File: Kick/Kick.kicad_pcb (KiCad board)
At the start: 4 copper layers, 127.8 x 66 mm, 11 parts, among them J1 CN1 / J11, J2 CN2 / J12, U0 NOIP1SN1300A-QTI, U1 NOIP1SN1300A-QTI, U2 NX3L4053, U3 NX3L4053, U4 MIC5504-1.8YM5

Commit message: added mounting holes for lens holder and rerouted long bottom traces from J11
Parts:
- added REF**: MountingHole_2.2mm_M2, MountingHole:MountingHole_2.2mm_M2, F.Cu at (130.9, 83.4)
- added REF**: MountingHole_2.2mm_M2, MountingHole:MountingHole_2.2mm_M2, F.Cu at (30.9, 63.4)
- added REF**: MountingHole_2.2mm_M2, MountingHole:MountingHole_2.2mm_M2, F.Cu at (50.9, 83.3)
- added REF**: MountingHole_2.2mm_M2, MountingHole:MountingHole_2.2mm_M2, F.Cu at (150.9, 63.4)
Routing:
- net /vddpix_0: track 57.8 -> 59.2 mm

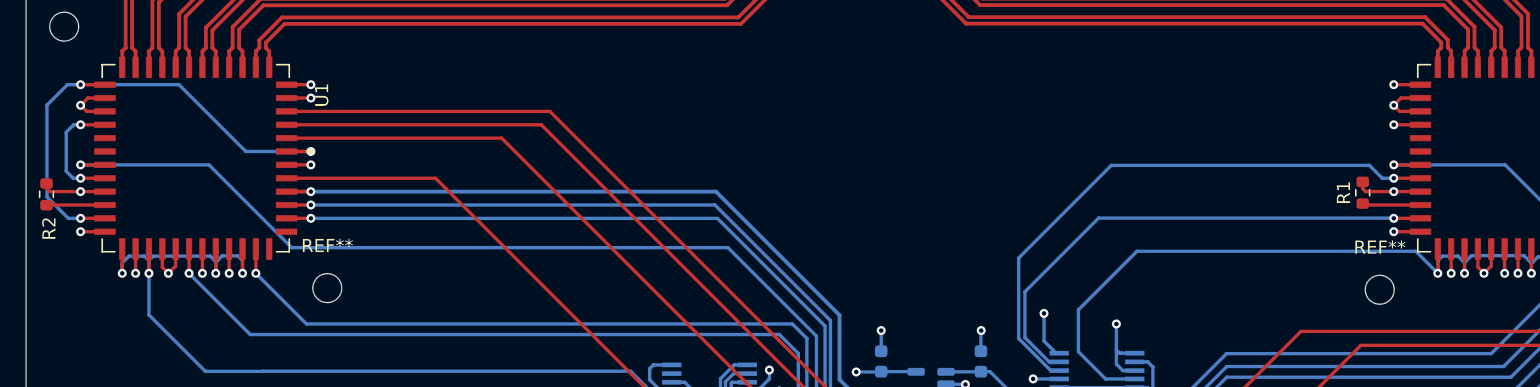
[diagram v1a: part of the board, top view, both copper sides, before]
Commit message: validated skew of single-ended signals with new clock delays
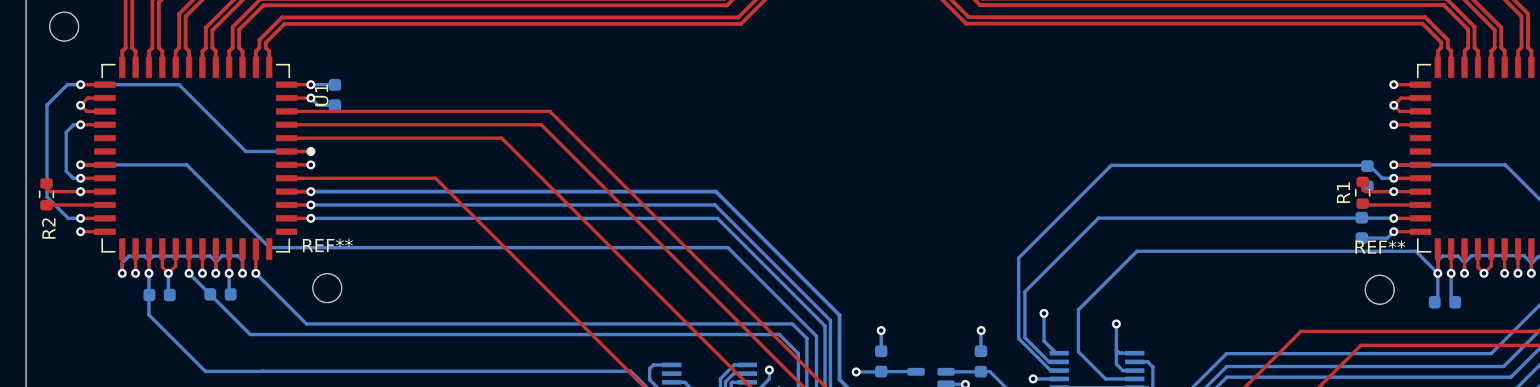
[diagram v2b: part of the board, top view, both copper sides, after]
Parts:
- added C3: C, Capacitor_SMD:C_0603_1608Metric, B.Cu at (129.5, 78.7)
- added C4: C, Capacitor_SMD:C_0603_1608Metric, B.Cu at (129.9, 74.8)
- added C5: C, Capacitor_SMD:C_0603_1608Metric, B.Cu at (135.8, 84.3)
- added C6: C, Capacitor_SMD:C_0603_1608Metric, B.Cu at (42.8, 83.8)
- added C7: C, Capacitor_SMD:C_0603_1608Metric, B.Cu at (51.5, 68.6)
- added C8: C, Capacitor_SMD:C_0603_1608Metric, B.Cu at (38.1, 83.8)
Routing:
- net GND: track 160.4 -> 173.0 mm
- net /vddpix_0: track 59.2 -> 61.5 mm
- net /vdd18_1: track 78.6 -> 80.5 mm

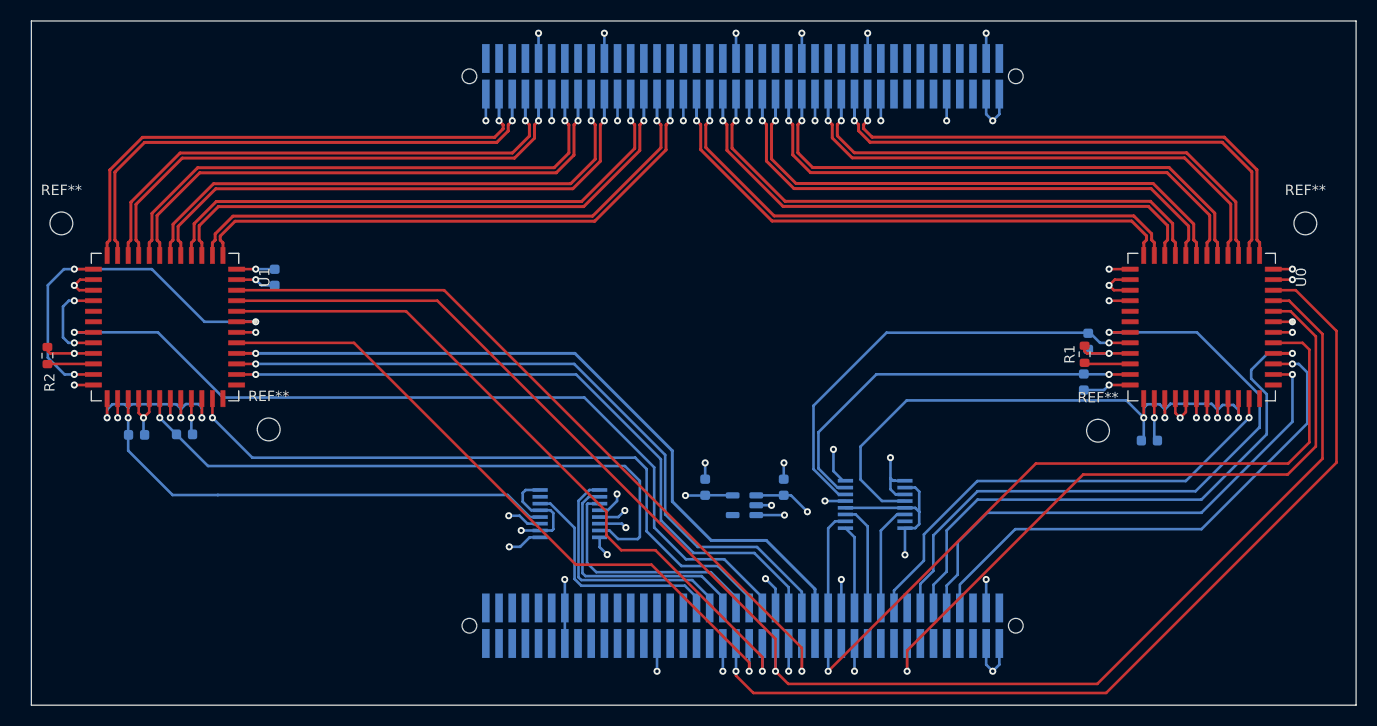
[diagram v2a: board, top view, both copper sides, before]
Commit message: length-matched spi signals
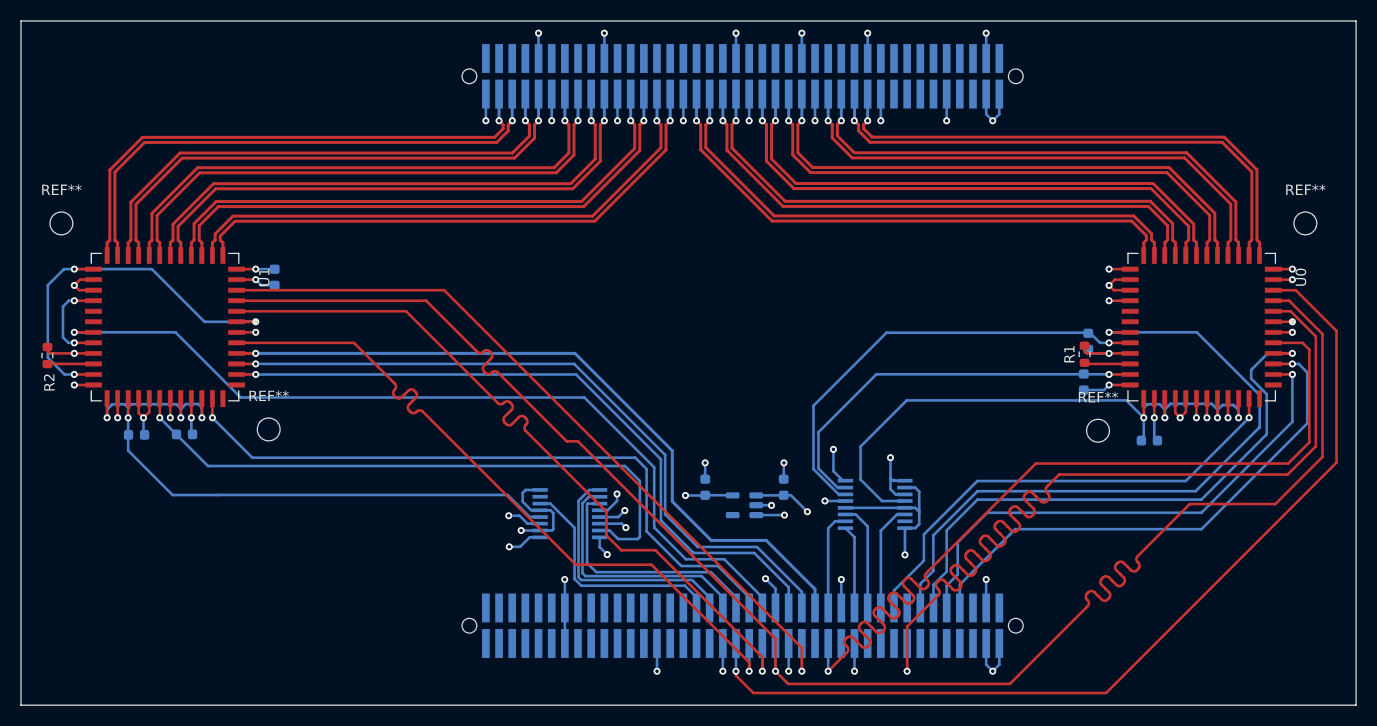
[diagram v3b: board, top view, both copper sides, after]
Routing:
- net /mosi: track 153.0 -> 179.6 mm
- net /ss_0: track 70.9 -> 86.8 mm
- net /miso: track 151.7 -> 162.1 mm
- net /ss_1: track 65.7 -> 69.4 mm
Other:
- board size 127.8 x 66 mm -> 128.8 x 66 mm

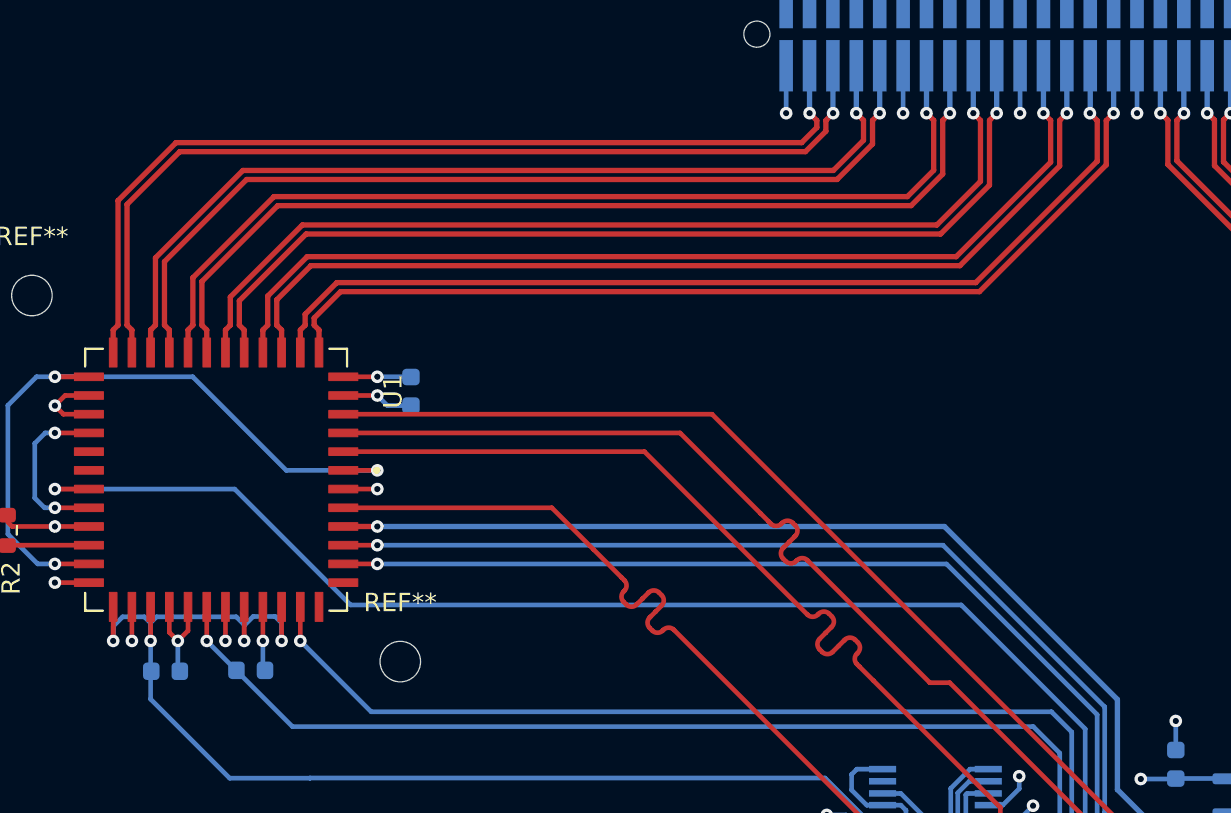
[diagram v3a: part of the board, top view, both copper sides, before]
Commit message: reasonable intra-pair skew on NOIP1
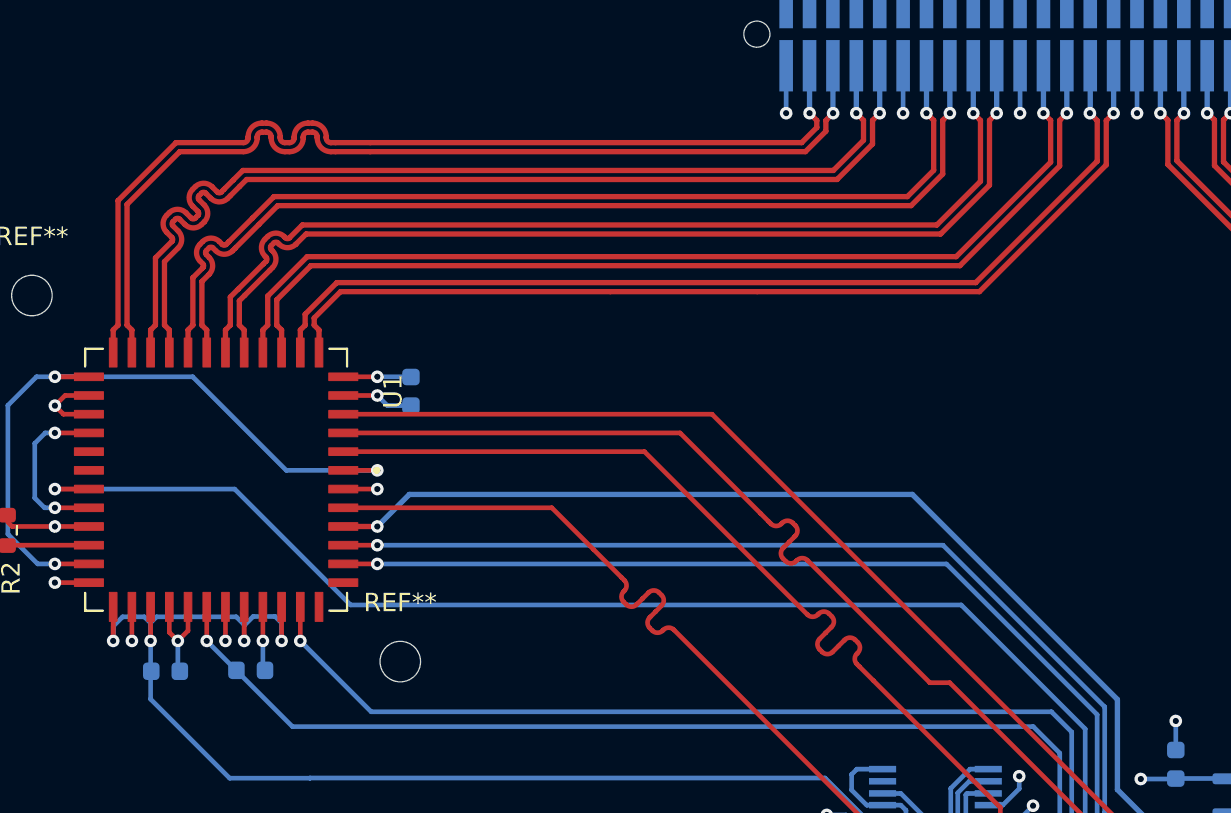
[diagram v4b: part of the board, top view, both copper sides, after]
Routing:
- net /dout3_1_P: track 50.5 -> 53.9 mm
- net /dout3_1_N: track 50.5 -> 53.9 mm
- net /sync1_P: track 51.5 -> 53.8 mm
- net /sync1_N: track 51.5 -> 53.8 mm
- net /resetn_1: track 69.9 -> 71.3 mm
- net /dout2_1_P: track 52.6 -> 53.9 mm
- net /dout2_1_N: track 52.6 -> 53.9 mm
- net /dout1_1_N: track 52.9 -> 53.9 mm
- net /dout1_1_P: track 52.9 -> 53.9 mm

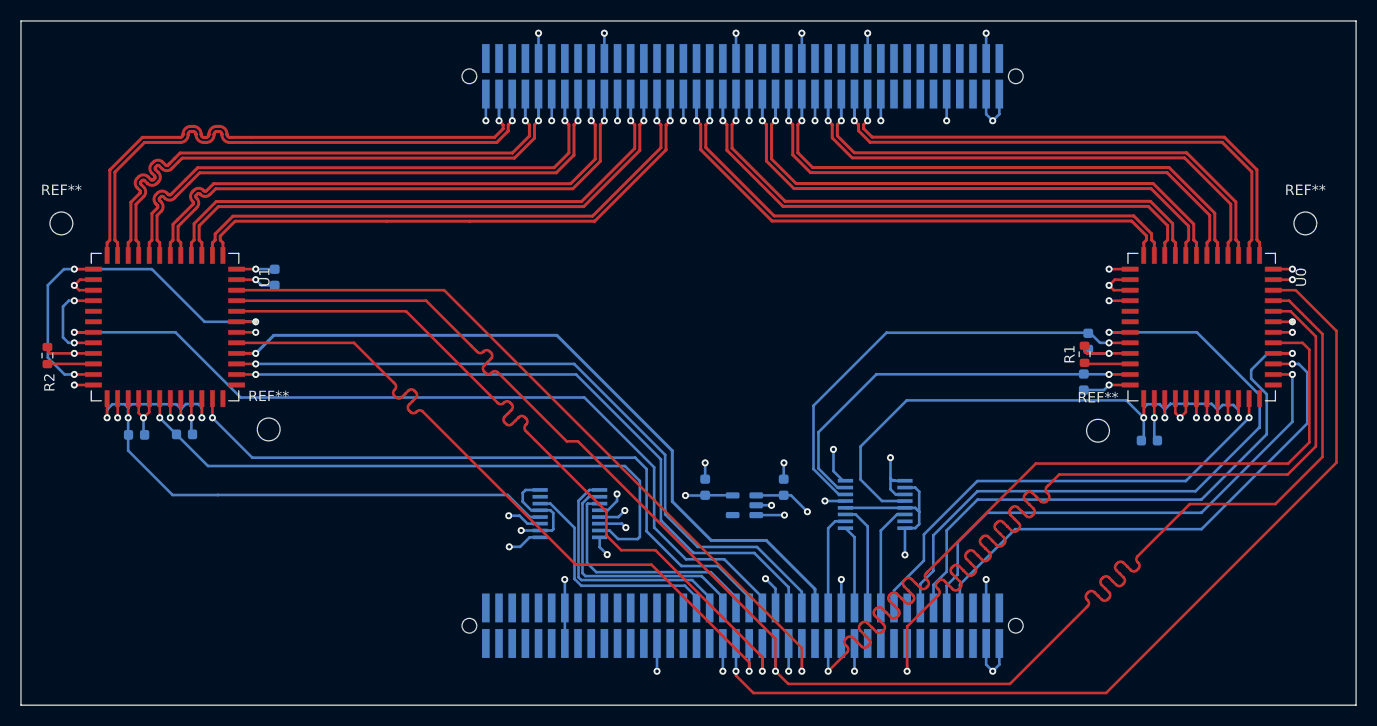
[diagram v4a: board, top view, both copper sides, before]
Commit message: replicated all length changes to NOIP0. no differential skew.
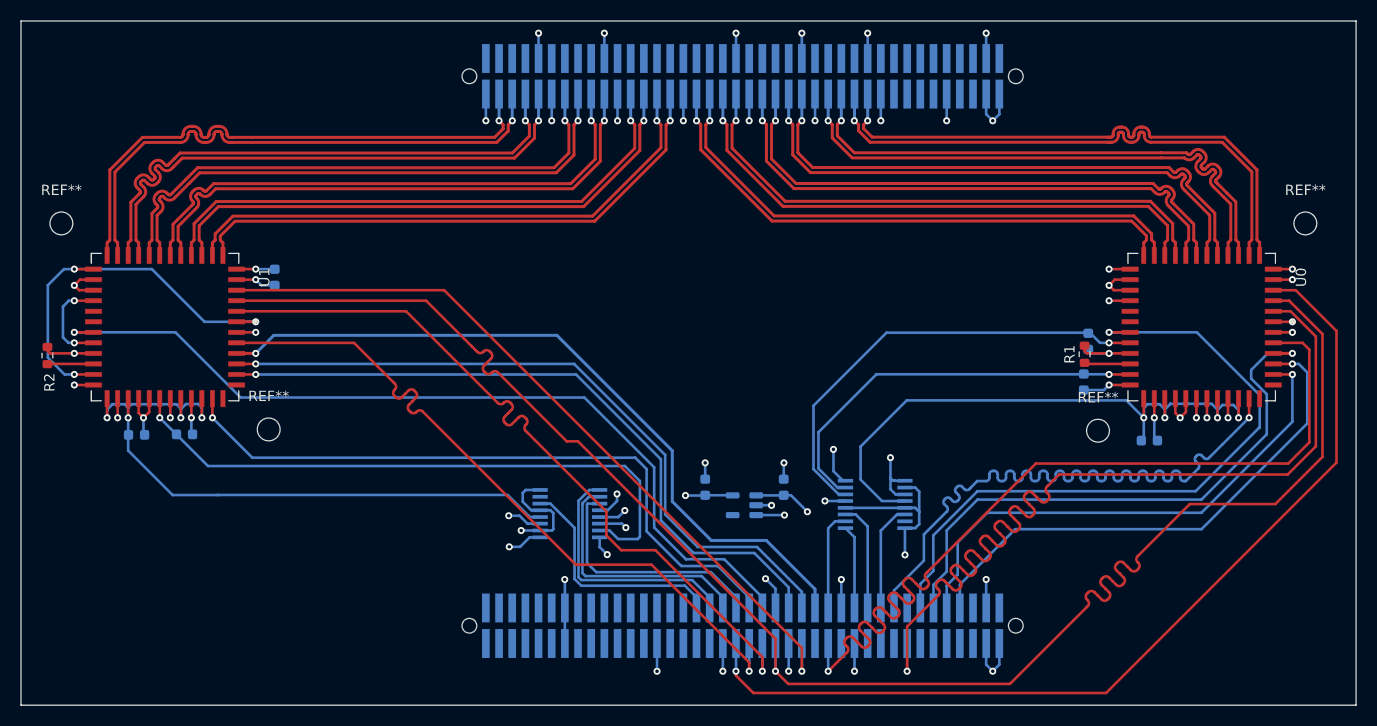
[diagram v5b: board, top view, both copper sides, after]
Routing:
- net /trigger0_0: track 46.2 -> 66.5 mm
- net /dout0_0_P: track 50.5 -> 53.9 mm
- net /dout0_0_N: track 50.5 -> 53.9 mm
- net /clkout0_N: track 51.5 -> 53.9 mm
- net /clkout0_P: track 51.5 -> 53.9 mm
- net /dout1_0_P: track 52.6 -> 53.9 mm
- net /dout1_0_N: track 52.6 -> 53.9 mm
- net /dout2_0_P: track 52.9 -> 53.9 mm
- net /dout2_0_N: track 52.9 -> 53.9 mm
